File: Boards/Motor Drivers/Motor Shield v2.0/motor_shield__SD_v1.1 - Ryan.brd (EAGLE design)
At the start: 77.1 x 52.1 mm, 25 parts

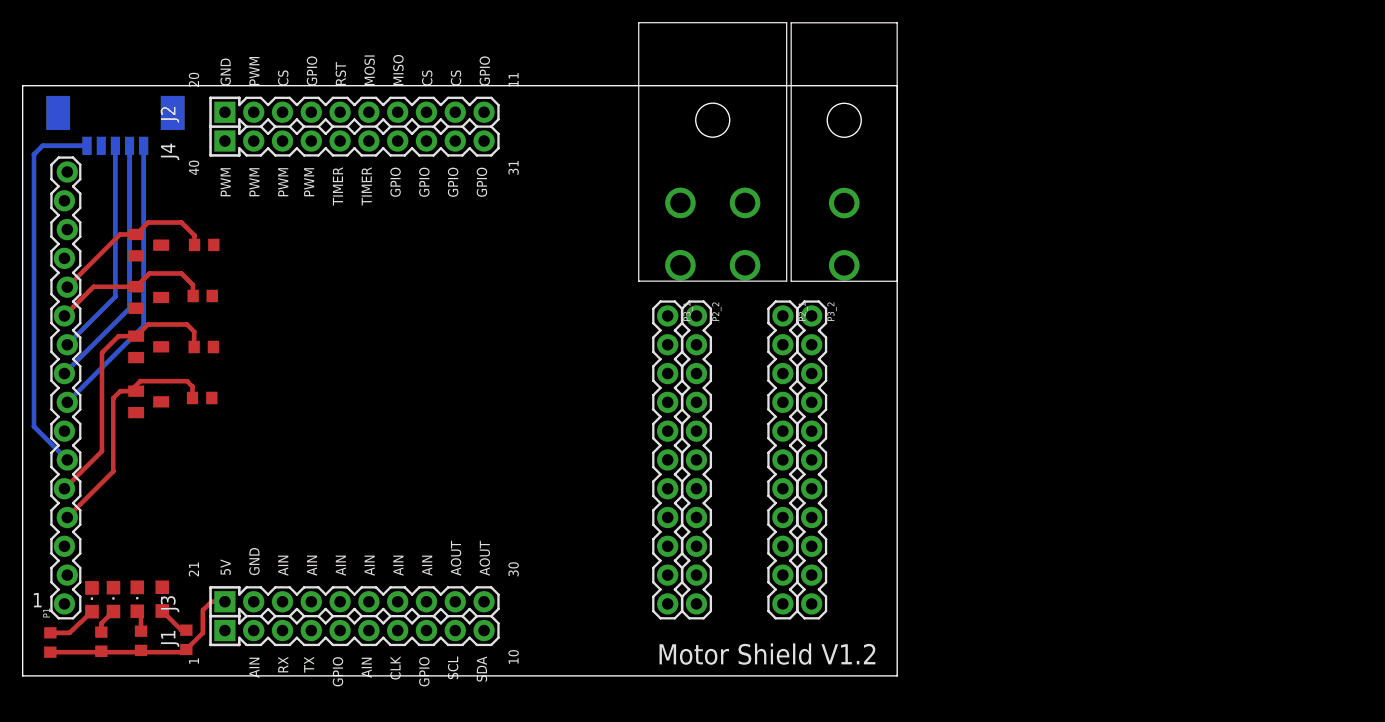
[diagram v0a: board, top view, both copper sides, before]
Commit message: Changes tiva headers, corrected ground and vol connections, layout finalizing. started routing
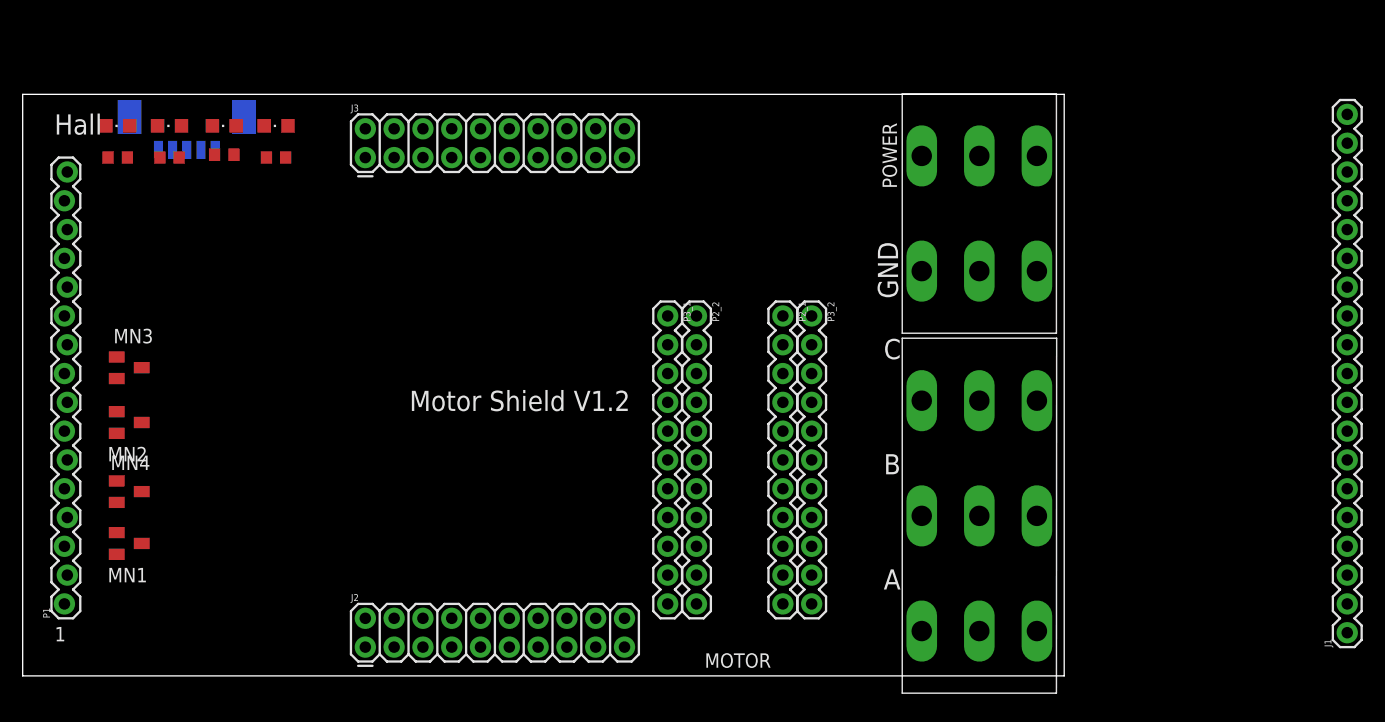
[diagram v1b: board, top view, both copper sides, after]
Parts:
- removed A1: (no value), EAGLE_BoosterPack_Library:4X10-BOOSTERPACK
- removed R5, R6, R7, R8: 1000, adafruit:R0603
- removed U$1: MOLEX2CON, TREC:MOLEX2CON
- removed U$2: MOLEX4CON, TREC1:MOLEX4CON
- added J1: (no value), SparkFun-Connectors:1X19
- added J2, J3: (no value), SparkFun-Connectors:2X10
- added MOTOR: PHOENIX_3POS, phoenixConn_3POS:PHOENIX_3POS
- added POWER: PHOENIX_2POS, phoenixConn_2POS:PHOENIX_2POS
- moved R4 43.5 mm to (17.8, 46.0), turned to 180 degrees
- moved R1 43.3 mm to (22.4, 45.7), turned to 180 degrees
- moved R3 43.2 mm to (8.38, 45.7), turned to 180 degrees
- moved R2 43.1 mm to (13.0, 45.7), turned to 180 degrees
- moved LED1 42.9 mm to (22.4, 48.5), turned to 90 degrees
- moved LED4 42.5 mm to (17.8, 48.5), turned to 90 degrees
- moved LED2 42.1 mm to (13.0, 48.5), turned to 90 degrees
- moved LED3 41.9 mm to (8.38, 48.5), turned to 90 degrees
- moved MN4 12.9 mm to (9.40, 16.3)
- moved MN1 12.6 mm to (9.40, 11.7)
- moved MN2 11.2 mm to (9.40, 22.4)
- moved MN3 10.9 mm to (9.40, 27.2)
- moved X1 6.31 mm to (14.5, 47.5)
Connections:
- removed net N$42: U$2.1
- removed net N$46: A1.1
- removed net N$47: A1.2
- removed net N$48: A1.3
- removed net N$49: A1.4
- removed net N$50: A1.5
- removed net N$51: A1.6
- removed net N$52: A1.7
- removed net N$53: A1.8
- removed net N$54: A1.9
- removed net N$55: A1.10
- removed net N$58: A1.23
- removed net N$59: A1.24
- removed net N$60: A1.25
- removed net N$61: A1.26
- removed net N$62: A1.27
- removed net N$63: A1.28
- removed net N$64: A1.29
- removed net N$66: A1.40
- removed net N$67: A1.39
- removed net N$68: A1.38
- removed net N$69: A1.37
- removed net N$70: A1.36
- removed net N$71: A1.35
- removed net N$72: A1.34
- removed net N$73: A1.33
- removed net N$74: A1.32
- removed net N$75: A1.31
- removed net N$76: A1.20
- removed net N$77: A1.19
- removed net N$78: A1.18
- removed net N$79: A1.17
- removed net N$80: A1.16
- removed net N$82: A1.14
- removed net N$83: A1.13
- removed net N$84: A1.12
- removed net N$85: A1.11
- new net 3.3V: J2.1
- new net 5V: J2.2
- new net N$12: J3.4
- new net N$13: J3.6
- new net N$14: J3.8
- new net N$17: J3.14
- new net N$18: J3.16
- new net N$19: J3.18
- new net N$20: J3.20
- new net N$21: J2.19
- new net N$22: J2.17
- new net N$23: J2.15
- new net N$24: J2.13
- new net N$25: J2.11
- new net N$26: J2.9
- new net N$27: J2.7
- new net N$28: J2.5
- new net N$29: J2.3
- new net N$3: J2.6
- new net N$31: J3.1
- new net N$32: J3.3
- new net N$33: J3.5
- new net N$34: J3.7
- new net N$35: J3.9
- new net N$36: J3.11
- new net N$37: J3.15
- new net N$38: J3.13
- new net N$39: J3.17
- new net N$4: J2.8
- new net N$40: J3.19
- new net N$5: J2.10
- new net N$6: J2.12
- new net N$7: J2.14
- new net N$8: J2.16
- new net N$9: J2.18
- new net RESET: J3.10
- net *INHIBIT: no longer R7.2
- net +5V: no longer A1.21
- net CURRENT_MONITOR: no longer R5.2
- net CURRENT_REF: no longer R8.2
- net DIRECTION: now also J2.20; no longer A1.30
- net FAULT_OUT: no longer R6.2
- net GND: now also J2.4, J3.2; no longer A1.22, R5.1, R6.1, R7.1, R8.1
- net HALL1: now also X1.3; no longer X1.5
- net HALL3: now also X1.5; no longer X1.3
- net HIGH_VOL: now also POWER.4, POWER.5, POWER.6; no longer U$1.1
- net MOTOR_A: now also MOTOR.1, MOTOR.2, MOTOR.3; no longer U$2.2
- net MOTOR_B: now also MOTOR.4, MOTOR.5, MOTOR.6; no longer U$2.3
- net MOTOR_C: now also MOTOR.7, MOTOR.8, MOTOR.9; no longer U$2.4
- net PWM: now also J3.12; no longer A1.15
- net PWR_GND: now also POWER.1, POWER.2, POWER.3; no longer U$1.2
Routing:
- net V+_HALL: track 33.2 -> 0.00 mm
- net HALL1: track 25.4 -> 0.00 mm
- net *INHIBIT: track 24.1 -> 0.00 mm
- net HALL2: track 22.5 -> 0.00 mm
- net CURRENT_MONITOR: track 21.5 -> 0.00 mm
- net HALL3: track 19.3 -> 0.00 mm
- net +5V: track 18.4 -> 0.00 mm
- net FAULT_OUT: track 14.9 -> 0.00 mm
- net CURRENT_REF: track 14.3 -> 0.00 mm
- net N$10: track 4.41 -> 0.00 mm
- net N$1: track 2.84 -> 0.00 mm
- net N$2: track 2.25 -> 0.00 mm
- net N$11: track 1.89 -> 0.00 mm
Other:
- board size 77.1 x 52.1 mm -> 91.9 x 51.3 mm
- board text added: "A"
- board text added: "B"
- board text added: "C"
- board text added: "GND"
